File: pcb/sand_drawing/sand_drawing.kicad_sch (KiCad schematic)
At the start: 39 parts, among them J0 12V GND, J1 Stepper1, J2 Stepper2, J3 Opto 1, J4 Opto 2, J5 UART, SW1 EN, SW2 IO0, U2 AMS1117-3.3, U3 ESP32-WROOM-32D

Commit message: Working on new vreg
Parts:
- removed U2: AMS1117-3.3, Package_TO_SOT_SMD:SOT-223, symbol Regulator_Linear:LD1117S33TR_SOT223
- added C3: 22µF/25V, Capacitors_SMD:C_1206, symbol Device:C
- added C4: 100nF/25V, Capacitors_SMD:C_1206, symbol Device:C
- added L1: 3.9µH, symbol Device:L
- added U2: AP63203WU, Package_TO_SOT_SMD:TSOT-23-6, symbol Regulator_Switching:AP63203WU
- C1: footprint Capacitors_SMD:C_0805 -> Capacitors_SMD:C_1206
- C2: value 10µF/25V -> 22µF/25V; footprint Capacitors_SMD:C_0805 -> Capacitors_SMD:C_1206
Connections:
- net +12V: now also U2.2 (EN), U2.3 (IN)
- net +3V3: now also C3.1, L1.2, U2.1 (FB)
- net GND: now also C3.2, U2.4 (GND)
- new net: C4.1, U2.5 (SW)
- new net: C4.2, L1.1, U2.6 (BST)
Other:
- moved on the sheet: A1, A2, C1, C2, C3, D1, D10, D11, D12, D13, D14, D15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

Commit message: v1.1 of the PCB nearly done.
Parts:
- removed D18: SS210 Schottky Diode, Diode_SMD:D_SMA, symbol Device:D_Schottky_Small
- added C3: 100nF/50V, Capacitor_SMD:C_0603_1608Metric, symbol Device:C
- C2: renamed from C1; value 10µF/25V -> 10µF/35V; footprint Capacitors_SMD:C_1206 -> Capacitor_SMD:C_1206_3216Metric
- C4: renamed from C2; footprint Capacitors_SMD:C_1206 -> Capacitor_SMD:C_1206_3216Metric
- C5: renamed from C3; footprint Capacitors_SMD:C_1206 -> Capacitor_SMD:C_1206_3216Metric
- C6: renamed from C4; value 100nF/25V -> 100nF/50V; footprint Capacitors_SMD:C_1206 -> Capacitor_SMD:C_0603_1608Metric
- L1: value 3.9µH -> 6.8µH; footprint (none) -> sand_drawing_parts:WURTH_6060
- renumbered C3 to C1, U2 to U1, U3 to U2
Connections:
- net +12V: now also C3.1
- net GND: now also C3.2
- net at C6.1, U1.5 (SW): now also L1.1
- net at C6.2, U1.6 (BST): no longer L1.1
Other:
- moved on the sheet: C2, C6, L1

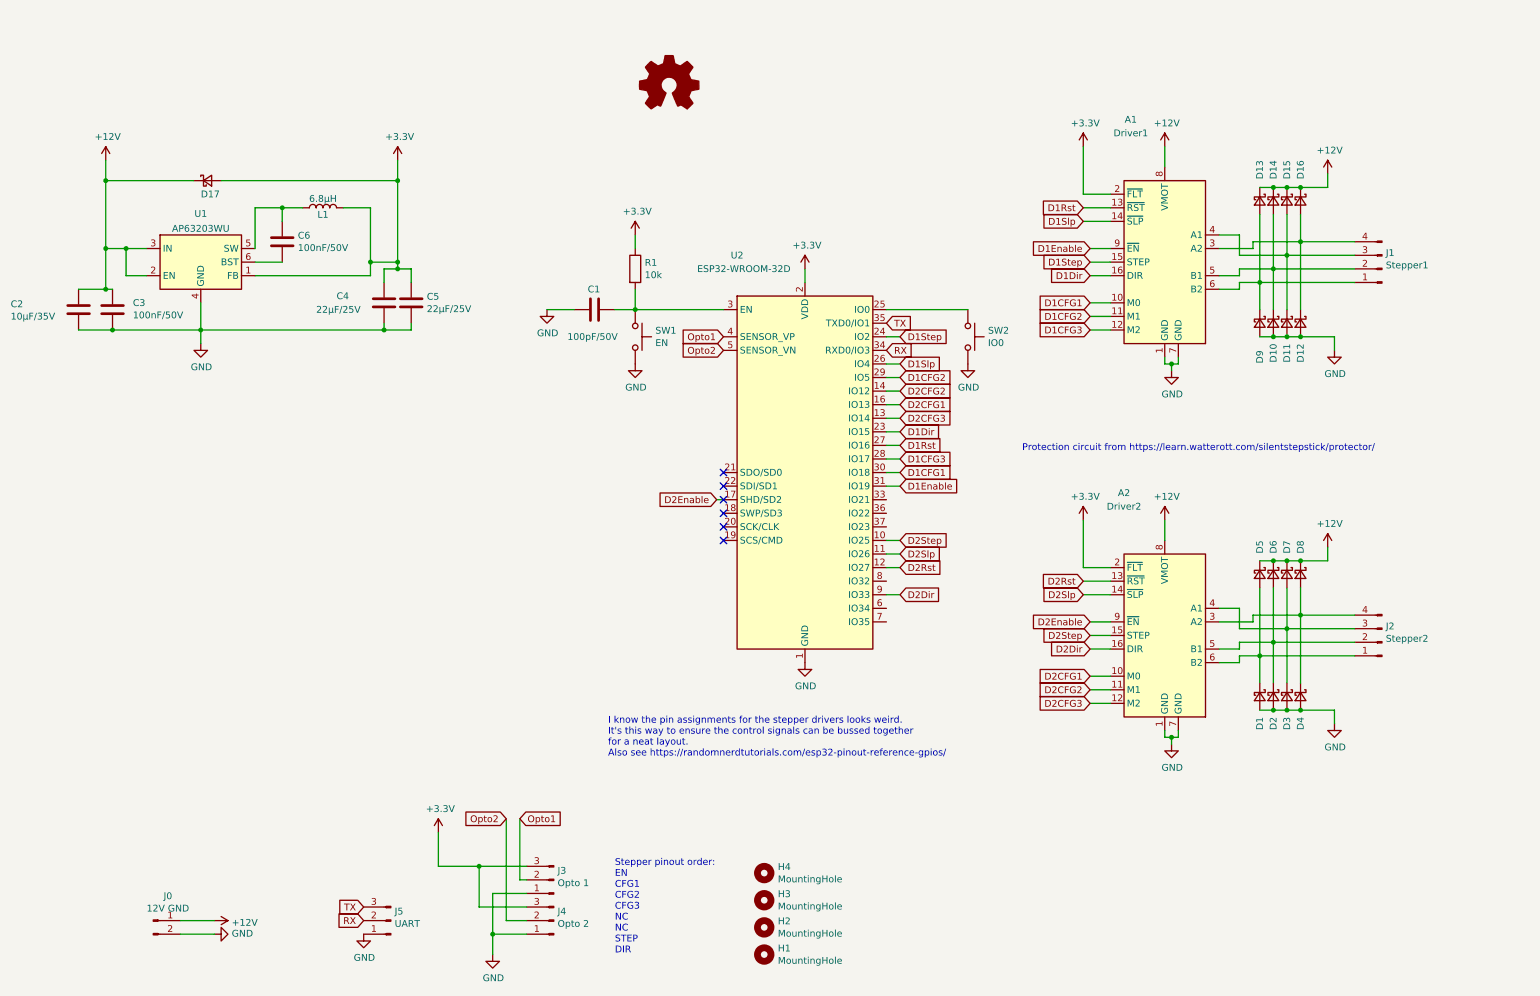
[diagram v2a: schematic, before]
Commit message: Updated to kicad v7.0.8.
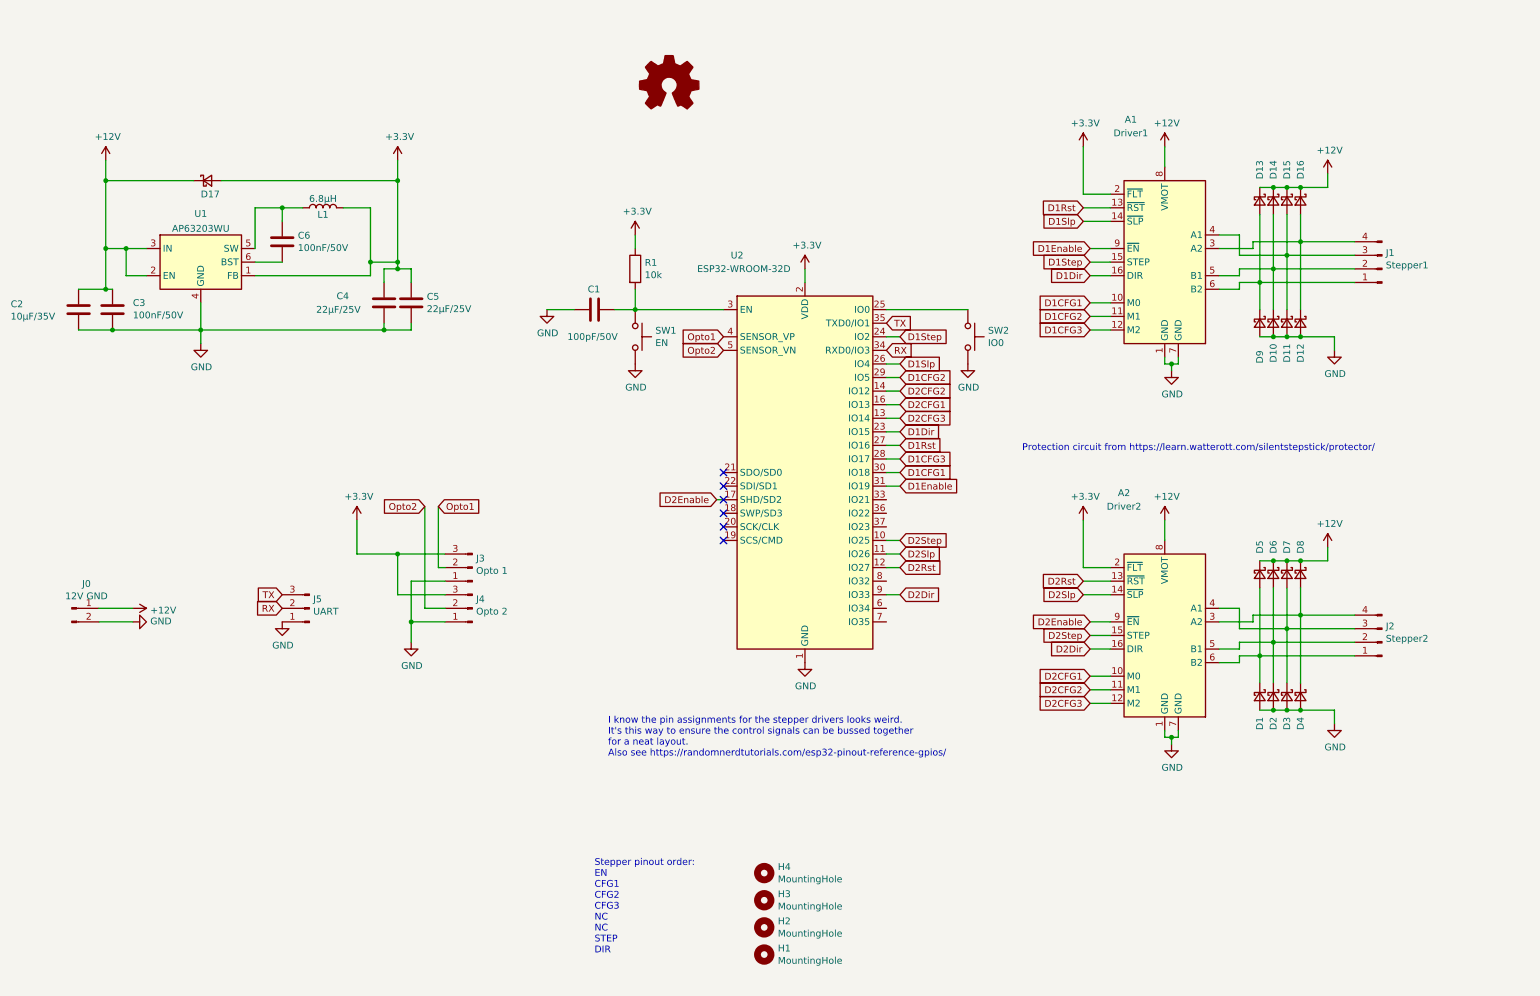
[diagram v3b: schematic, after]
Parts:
- C1: footprint Capacitors_SMD:C_0805 -> Capacitor_SMD:C_0805_2012Metric
- L1: BOM (none) -> Würth PART 744 393 460 68
- SW1, SW2: footprint Buttons_Switches_THT:SW_PUSH_6mm -> Button_Switch_THT:SW_PUSH_6mm
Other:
- moved on the sheet: J0, J3, J4, J5

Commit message: Update footprints.
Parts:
- H1, H2, H3, H4: footprint Mounting_Holes:MountingHole_3.2mm_M3 -> MountingHole:MountingHole_3.2mm_M3
- J0: footprint Connectors_Phoenix:PhoenixContact_MCV-G_02x3.50mm_Vertical -> Connector_Phoenix_MC:PhoenixContact_MCV_1,5_2-G-3.5_1x02_P3.50mm_Vertical
- J1, J2: footprint Connectors_Phoenix:PhoenixContact_MCV-G_04x3.50mm_Vertical -> Connector_Phoenix_MC:PhoenixContact_MCV_1,5_4-G-3.5_1x04_P3.50mm_Vertical
- J3, J4: footprint Connectors_Phoenix:PhoenixContact_MCV-G_03x3.50mm_Vertical -> Connector_Phoenix_MC:PhoenixContact_MCV_1,5_3-G-3.5_1x03_P3.50mm_Vertical
- J5: footprint Socket_Strips:Socket_Strip_Straight_1x03_Pitch2.54mm -> Connector_PinSocket_2.54mm:PinSocket_1x03_P2.54mm_Vertical
- R1: footprint Resistors_SMD:R_0603 -> Resistor_SMD:R_0603_1608Metric
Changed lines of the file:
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@@
       (effects (font (size 1.27 1.27)) (justify right))
     )
-    (property "Footprint" "Connectors_Phoenix:PhoenixContact_MCV-G_04x3.50mm_Vertical" (at 273.05 63.5 0)
+    (property "Footprint" "Connector_Phoenix_MC:PhoenixContact_MCV_1,5_4-G-3.5_1x04_P3.50mm_Vertical" (at 273.05 63.5 0)
       (effects (font (size 1.27 1.27)) hide)
     )
@@
       (effects (font (size 1.27 1.27)) (justify right))
     )
-    (property "Footprint" "Connectors_Phoenix:PhoenixContact_MCV-G_04x3.50mm_Vertical" (at 273.05 133.35 0)
+    (property "Footprint" "Connector_Phoenix_MC:PhoenixContact_MCV_1,5_4-G-3.5_1x04_P3.50mm_Vertical" (at 273.05 133.35 0)
       (effects (font (size 1.27 1.27)) hide)
     )
@@
       (effects (font (size 1.27 1.27)) (justify right))
     )
-    (property "Footprint" "Connectors_Phoenix:PhoenixContact_MCV-G_03x3.50mm_Vertical" (at 102.87 119.38 0)
+    (property "Footprint" "Connector_Phoenix_MC:PhoenixContact_MCV_1,5_3-G-3.5_1x03_P3.50mm_Vertical" (at 102.87 119.38 0)
       (effects (font (size 1.27 1.27)) hide)
     )
@@
       (effects (font (size 1.27 1.27)) (justify right))
     )
-    (property "Footprint" "Connectors_Phoenix:PhoenixContact_MCV-G_03x3.50mm_Vertical" (at 102.87 127 0)
+    (property "Footprint" "Connector_Phoenix_MC:PhoenixContact_MCV_1,5_3-G-3.5_1x03_P3.50mm_Vertical" (at 102.87 127 0)
       (effects (font (size 1.27 1.27)) hide)
     )
@@
       (effects (font (size 1.27 1.27)))
     )
-    (property "Footprint" "Connectors_Phoenix:PhoenixContact_MCV-G_02x3.50mm_Vertical" (at 27.94 127 0)
+    (property "Footprint" "Connector_Phoenix_MC:PhoenixContact_MCV_1,5_2-G-3.5_1x02_P3.50mm_Vertical" (at 27.94 127 0)
       (effects (font (size 1.27 1.27)) hide)
     )
@@
       (effects (font (size 1.27 1.27)) (justify right))
     )
-    (property "Footprint" "Socket_Strips:Socket_Strip_Straight_1x03_Pitch2.54mm" (at 72.39 127 0)
+    (property "Footprint" "Connector_PinSocket_2.54mm:PinSocket_1x03_P2.54mm_Vertical" (at 72.39 127 0)
       (effects (font (size 1.27 1.27)) hide)
     )
@@
       (effects (font (size 1.27 1.27)) (justify left))
     )
-    (property "Footprint" "Mounting_Holes:MountingHole_3.2mm_M3" (at 157.48 191.77 0)
+    (property "Footprint" "MountingHole:MountingHole_3.2mm_M3" (at 157.48 191.77 0)
       (effects (font (size 1.27 1.27)) hide)
     )
@@
       (effects (font (size 1.27 1.27)) (justify left))
     )
-    (property "Footprint" "Mounting_Holes:MountingHole_3.2mm_M3" (at 157.48 186.69 0)
+    (property "Footprint" "MountingHole:MountingHole_3.2mm_M3" (at 157.48 186.69 0)
       (effects (font (size 1.27 1.27)) hide)
     )
@@
       (effects (font (size 1.27 1.27)) (justify left))
     )
-    (property "Footprint" "Mounting_Holes:MountingHole_3.2mm_M3" (at 157.48 181.61 0)
+    (property "Footprint" "MountingHole:MountingHole_3.2mm_M3" (at 157.48 181.61 0)
       (effects (font (size 1.27 1.27)) hide)
     )
@@
       (effects (font (size 1.27 1.27)) (justify left))
     )
-    (property "Footprint" "Mounting_Holes:MountingHole_3.2mm_M3" (at 157.48 176.53 0)
+    (property "Footprint" "MountingHole:MountingHole_3.2mm_M3" (at 157.48 176.53 0)
       (effects (font (size 1.27 1.27)) hide)
     )
@@
       (effects (font (size 1.27 1.27)) (justify left))
     )
-    (property "Footprint" "Resistors_SMD:R_0603" (at 131.572 63.5 90)
-      (effects (font (size 1.27 1.27)) hide)
-    )
+    (property "Footprint" "Resistor_SMD:R_0603_1608Metric" (at 131.572 63.5 90)
+      (effects (font (size 1.27 1.27)) hide)
+    )

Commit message: PCB v1.1
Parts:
- A1, A2, H1, H2, H3, H4, J0, J1, J2, J3, J4, J5, LOGO1, SW1, SW2: now left out of the parts list
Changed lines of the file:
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@@
   )
   (symbol (lib_id "pololu_breakout_tmc2100:Pololu_Breakout_DRV8825_copy") (at 232.41 59.69 0) (unit 1)
-    (in_bom yes) (on_board yes) (dnp no)
+    (in_bom no) (on_board yes) (dnp no)
     (property "Reference" "A1" (at 226.06 35.56 0)
       (effects (font (size 1.27 1.27)))
@@
   )
   (symbol (lib_id "pololu_breakout_tmc2100:Pololu_Breakout_DRV8825_copy") (at 232.41 129.54 0) (unit 1)
-    (in_bom yes) (on_board yes) (dnp no)
+    (in_bom no) (on_board yes) (dnp no)
     (property "Reference" "A2" (at 224.79 105.41 0)
       (effects (font (size 1.27 1.27)))
@@
   )
   (symbol (lib_id "Connector:Conn_01x04_Male") (at 273.05 63.5 180) (unit 1)
-    (in_bom yes) (on_board yes) (dnp no)
+    (in_bom no) (on_board yes) (dnp no)
     (property "Reference" "J1" (at 273.7612 60.5028 0)
       (effects (font (size 1.27 1.27)) (justify right))
@@
   )
   (symbol (lib_id "Connector:Conn_01x04_Male") (at 273.05 133.35 180) (unit 1)
-    (in_bom yes) (on_board yes) (dnp no)
+    (in_bom no) (on_board yes) (dnp no)
     (property "Reference" "J2" (at 273.7612 130.3528 0)
       (effects (font (size 1.27 1.27)) (justify right))
@@
   )
   (symbol (lib_id "Connector:Conn_01x03_Male") (at 102.87 119.38 180) (unit 1)
-    (in_bom yes) (on_board yes) (dnp no)
+    (in_bom no) (on_board yes) (dnp no)
     (property "Reference" "J3" (at 103.5812 117.6528 0)
       (effects (font (size 1.27 1.27)) (justify right))
@@
   )
   (symbol (lib_id "Connector:Conn_01x03_Male") (at 102.87 127 180) (unit 1)
-    (in_bom yes) (on_board yes) (dnp no)
+    (in_bom no) (on_board yes) (dnp no)
     (property "Reference" "J4" (at 103.5812 125.2728 0)
       (effects (font (size 1.27 1.27)) (justify right))
@@
   )
   (symbol (lib_id "Connector:Conn_01x02_Male") (at 27.94 127 0) (unit 1)
-    (in_bom yes) (on_board yes) (dnp no)
+    (in_bom no) (on_board yes) (dnp no)
     (property "Reference" "J0" (at 30.6832 122.4026 0)
       (effects (font (size 1.27 1.27)))
@@
   )
   (symbol (lib_id "Connector:Conn_01x03_Male") (at 72.39 127 180) (unit 1)
-    (in_bom yes) (on_board yes) (dnp no)
+    (in_bom no) (on_board yes) (dnp no)
     (property "Reference" "J5" (at 73.1012 125.2728 0)
       (effects (font (size 1.27 1.27)) (justify right))
@@
   )
   (symbol (lib_id "Mechanical:MountingHole") (at 157.48 191.77 0) (unit 1)
-    (in_bom yes) (on_board yes) (dnp no)
+    (in_bom no) (on_board yes) (dnp no)
     (property "Reference" "H1" (at 160.02 190.6016 0)
       (effects (font (size 1.27 1.27)) (justify left))
@@
   )
   (symbol (lib_id "Mechanical:MountingHole") (at 157.48 186.69 0) (unit 1)
-    (in_bom yes) (on_board yes) (dnp no)
+    (in_bom no) (on_board yes) (dnp no)
     (property "Reference" "H2" (at 160.02 185.5216 0)
       (effects (font (size 1.27 1.27)) (justify left))
@@
   )
   (symbol (lib_id "Mechanical:MountingHole") (at 157.48 181.61 0) (unit 1)
-    (in_bom yes) (on_board yes) (dnp no)
+    (in_bom no) (on_board yes) (dnp no)
     (property "Reference" "H3" (at 160.02 180.4416 0)
       (effects (font (size 1.27 1.27)) (justify left))
@@
   )
   (symbol (lib_id "Mechanical:MountingHole") (at 157.48 176.53 0) (unit 1)
-    (in_bom yes) (on_board yes) (dnp no)
+    (in_bom no) (on_board yes) (dnp no)
     (property "Reference" "H4" (at 160.02 175.3616 0)
       (effects (font (size 1.27 1.27)) (justify left))
@@
   )
   (symbol (lib_id "Graphic:Logo_Open_Hardware_Small") (at 139.7 29.21 0) (unit 1)
-    (in_bom yes) (on_board yes) (dnp no)
+    (in_bom no) (on_board yes) (dnp no)
     (property "Reference" "LOGO1" (at 139.7 22.225 0)
       (effects (font (size 1.27 1.27)) hide)
@@
   )
   (symbol (lib_id "Switch:SW_Push") (at 133.35 76.2 270) (unit 1)
-    (in_bom yes) (on_board yes) (dnp no)
+    (in_bom no) (on_board yes) (dnp no)
     (property "Reference" "SW1" (at 137.1092 75.0316 90)
       (effects (font (size 1.27 1.27)) (justify left))
@@
   )
   (symbol (lib_id "Switch:SW_Push") (at 195.58 76.2 270) (unit 1)
-    (in_bom yes) (on_board yes) (dnp no)
+    (in_bom no) (on_board yes) (dnp no)
     (property "Reference" "SW2" (at 199.3392 75.0316 90)
       (effects (font (size 1.27 1.27)) (justify left))

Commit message: Tweaks to PCB. Finding parts.
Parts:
- C1: value 100pF/50V -> 50V 100pF C0G ±5%; MPN (none) -> VJ0402A101JXACW1BC; Package (none) -> 0805
- C2, C4, C5: Package (none) -> 1206
- C3, C6: Package (none) -> 0603
- D1, D10, D11, D12, D13, D14, D15, D16, D17, D2, D3, D4, D5, D6, D7, D8, D9: value SS210 Schottky Diode -> 100V 850mV@2A Schottky Diode; MPN (none) -> SS210

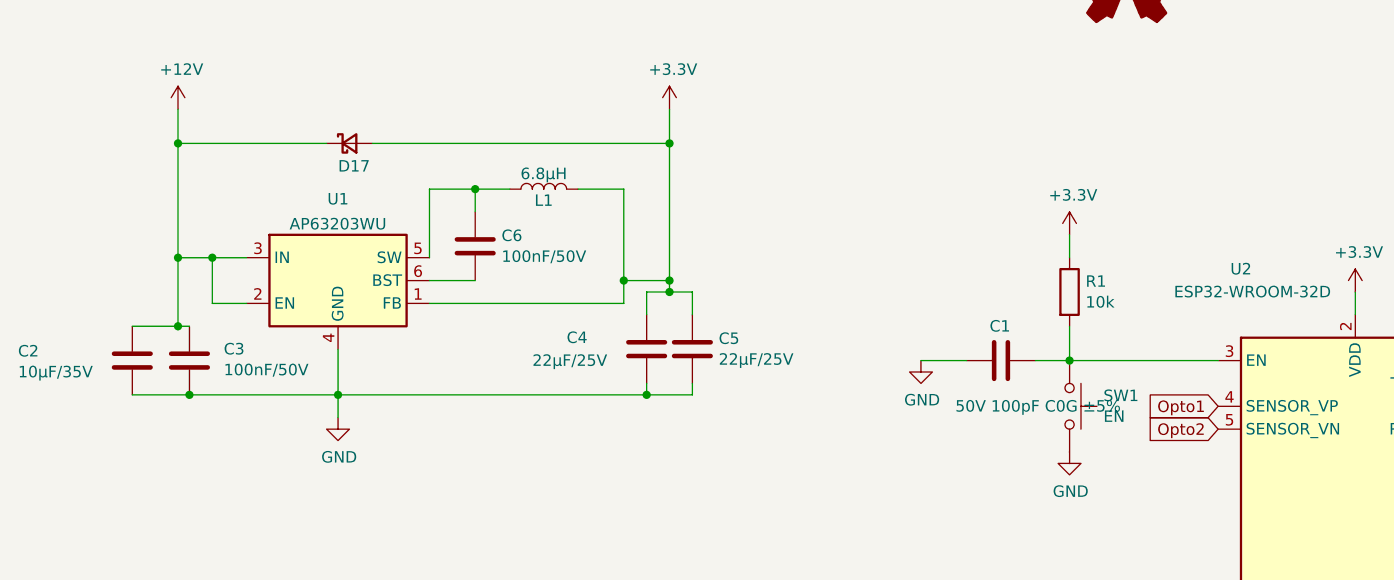
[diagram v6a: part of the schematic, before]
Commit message: Updated part numbers and footprints.
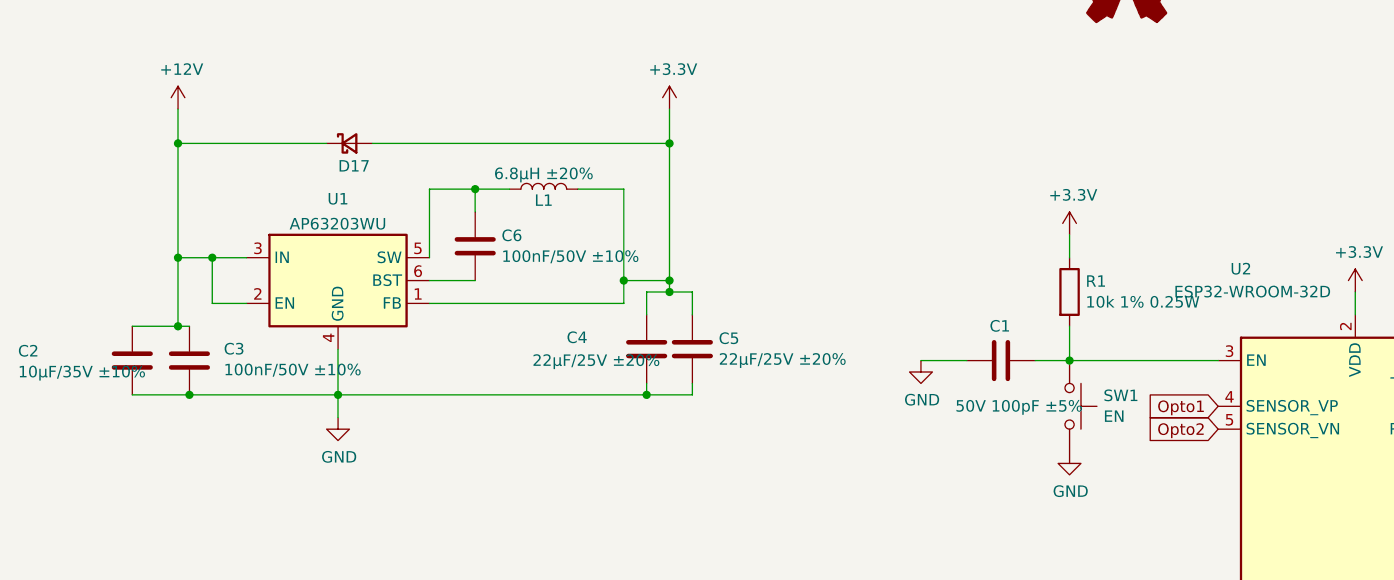
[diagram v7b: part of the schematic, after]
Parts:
- C1: value 50V 100pF C0G ±5% -> 50V 100pF ±5%; MPN VJ0402A101JXACW1BC -> CL21C101JBANNNC
- C2: value 10µF/35V -> 10µF/35V ±10%; MPN (none) -> CGA5L1X7R1V106K160AE
- C3, C6: value 100nF/50V -> 100nF/50V ±10%; MPN (none) -> CGA3E2X7R1H104K080AA
- C4, C5: value 22µF/25V -> 22µF/25V ±20%; MPN (none) -> C3216X5R1E226M160AB
- D1, D10, D11, D12, D13, D14, D15, D16, D17, D2, D3, D4, D5, D6, D7, D8, D9: footprint Diode_SMD:D_SMA -> Diode_SMD:D_SMB; MPN SS210 -> Taiwan Semiconductor SS210; Package (none) -> SMB
- L1: value 6.8µH -> 6.8µH ±20%; MPN (none) -> Wurth 74439346068; Package (none) -> 6060
- R1: value 10k -> 10k 1% 0.25W; MPN (none) -> CRGP0603F10K; Package (none) -> 0603
- U1: footprint Package_TO_SOT_SMD:TSOT-23-6 -> sand_drawing_parts:TSOT-26-6; MPN (none) -> AP63203WU-7; Package (none) -> TSOT-26-6
- U2: MPN (none) -> ESP32-WROOM-32D

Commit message: PCB DRC and label fixes.
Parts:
- U2: MPN ESP32-WROOM-32D -> ESP32-WROOM-32D-N16
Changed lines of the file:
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@@
       (effects (font (size 1.27 1.27)) hide)
     )
-    (property "MPN" "ESP32-WROOM-32D" (at 165.1 101.6 0)
+    (property "MPN" "ESP32-WROOM-32D-N16" (at 165.1 101.6 0)
       (effects (font (size 1.27 1.27)) hide)
     )
